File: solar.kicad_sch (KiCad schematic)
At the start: 7 parts

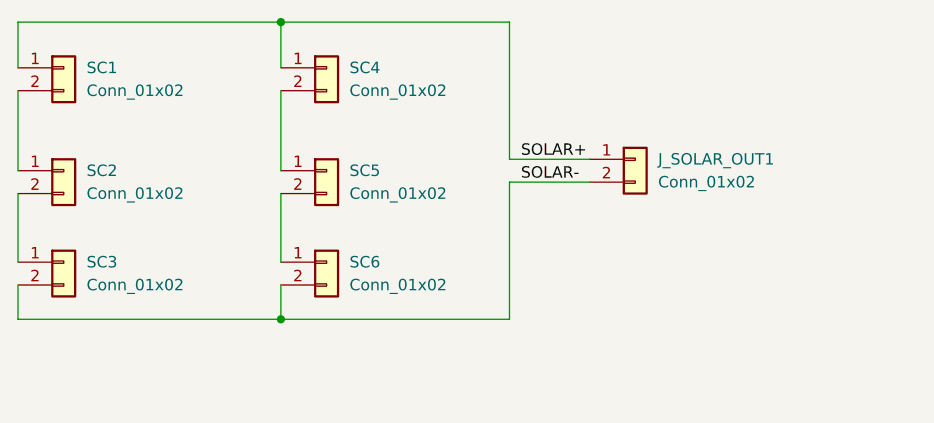
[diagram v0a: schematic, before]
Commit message: add temperature sensor
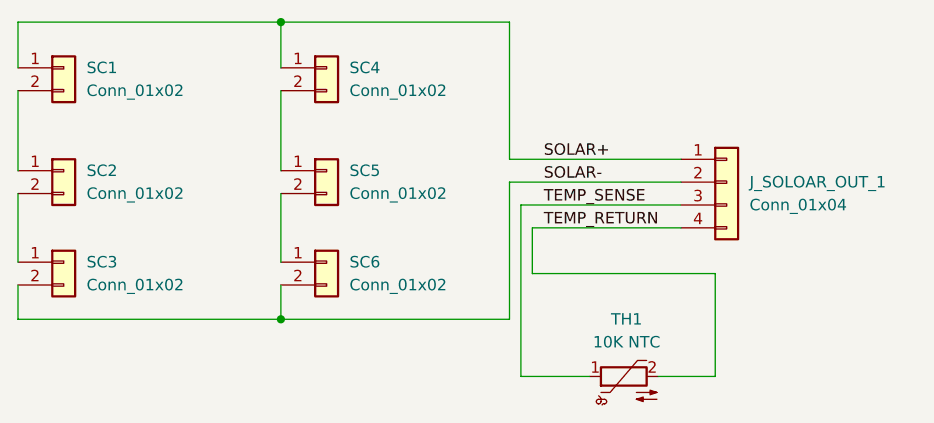
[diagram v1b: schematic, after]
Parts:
- removed J_SOLAR_OUT1: Conn_01x02, Connector_JST:JST_PH_S2B-PH-K_1x02_P2.00mm_Horizontal, symbol Connector_Generic:Conn_01x02
- added J_SOLOAR_OUT_1: Conn_01x04, Connector_JST:JST_PH_S4B-PH-K_1x04_P2.00mm_Horizontal, symbol Connector_Generic:Conn_01x04
- added TH1: 10K NTC, Diode_THT:D_DO-35_SOD27_P7.62mm_Horizontal, symbol Device:Thermistor_NTC
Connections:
- net SOLAR+: now also J_SOLOAR_OUT_1.1 (Pin_1)
- net SOLAR-: now also J_SOLOAR_OUT_1.2 (Pin_2)
- new net TEMP_RETURN: J_SOLOAR_OUT_1.4 (Pin_4), TH1.2
- new net TEMP_SENSE: J_SOLOAR_OUT_1.3 (Pin_3), TH1.1
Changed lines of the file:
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@@
 	(wire
 		(pts
-			(xy 186.69 100.33) (xy 177.8 100.33)
+			(xy 179.07 124.46) (xy 186.69 124.46)
 		)
 		(stroke
@@
 	(wire
 		(pts
+			(xy 200.66 124.46) (xy 200.66 113.03)
+		)
+		(stroke
+			(width 0)
+			(type default)
+		)
+	)
+	(wire
+		(pts
+			(xy 179.07 105.41) (xy 179.07 124.46)
+		)
+		(stroke
+			(width 0)
+			(type default)
+		)
+	)
+	(wire
+		(pts
 			(xy 152.4 114.3) (xy 152.4 118.11)
 		)
@@
 	(wire
 		(pts
+			(xy 180.34 107.95) (xy 196.85 107.95)
+		)
+		(stroke
+			(width 0)
+			(type default)
+		)
+	)
+	(wire
+		(pts
 			(xy 152.4 92.71) (xy 152.4 101.6)
 		)
@@
 	(wire
 		(pts
+			(xy 177.8 102.87) (xy 196.85 102.87)
+		)
+		(stroke
+			(width 0)
+			(type default)
+		)
+	)
+	(wire
+		(pts
+			(xy 194.31 124.46) (xy 200.66 124.46)
+		)
+		(stroke
+			(width 0)
+			(type default)
+		)
+	)
+	(wire
+		(pts
 			(xy 123.19 118.11) (xy 152.4 118.11)
 		)
@@
 	(wire
 		(pts
-			(xy 186.69 102.87) (xy 177.8 102.87)
+			(xy 177.8 100.33) (xy 196.85 100.33)
 		)
 		(stroke
@@
 	(wire
 		(pts
+			(xy 179.07 105.41) (xy 196.85 105.41)
+		)
+		(stroke
+			(width 0)
+			(type default)
+		)
+	)
+	(wire
+		(pts
+			(xy 180.34 113.03) (xy 180.34 107.95)
+		)
+		(stroke
+			(width 0)
+			(type default)
+		)
+	)
+	(wire
+		(pts
+			(xy 200.66 113.03) (xy 180.34 113.03)
+		)
+		(stroke
+			(width 0)
+			(type default)
+		)
+	)
+	(wire
+		(pts
 			(xy 177.8 102.87) (xy 177.8 118.11)
 		)
@@
 		)
 	)
-	(label "SOLAR+"
-		(at 179.07 100.33 0)
+	(label "TEMP_RETURN"
+		(at 181.61 107.95 0)
 		(effects
 			(font
@@
 		)
 	)
+	(label "SOLAR+"
+		(at 181.61 100.33 0)
+		(effects
+			(font
+				(size 1.27 1.27)
+			)
+			(justify left bottom)
+		)
+	)
+	(label "TEMP_SENSE"
+		(at 181.61 105.41 0)
+		(effects
+			(font
+				(size 1.27 1.27)
+			)
+			(justify left bottom)
+		)
+	)
 	(label "SOLAR-"
-		(at 179.07 102.87 0)
+		(at 181.61 102.87 0)
 		(effects
 			(font
@@
 	)
 	(symbol
-		(lib_id "Connector_Generic:Conn_01x02")
-		(at 191.77 100.33 0)
+		(lib_id "Device:Thermistor_NTC")
+		(at 190.5 124.46 90)
 		(unit 1)
 		(body_style 1)
@@
 		(dnp no)
 		(fields_autoplaced yes)
-		(property "Reference" "J_SOLAR_OUT1"
-			(at 194.31 100.3299 0)
-			(show_name no)
-			(do_not_autoplace no)
-			(effects
-				(font
-					(size 1.27 1.27)
-				)
-				(justify left)
-			)
-		)
-		(property "Value" "Conn_01x02"
-			(at 194.31 102.8699 0)
-			(show_name no)
-			(do_not_autoplace no)
-			(effects
-				(font
-					(size 1.27 1.27)
-				)
-				(justify left)
-			)
-		)
-		(property "Footprint" "Connector_JST:JST_PH_S2B-PH-K_1x02_P2.00mm_Horizontal"
-			(at 191.77 100.33 0)
+		(property "Reference" "TH1"
+			(at 190.8175 118.11 90)
+			(show_name no)
+			(do_not_autoplace no)
+			(effects
+				(font
+					(size 1.27 1.27)
+				)
+			)
+		)
+		(property "Value" "10K NTC"
+			(at 190.8175 120.65 90)
+			(show_name no)
+			(do_not_autoplace no)
+			(effects
+				(font
+					(size 1.27 1.27)
+				)
+			)
+		)
+		(property "Footprint" "Diode_THT:D_DO-35_SOD27_P7.62mm_Horizontal"
+			(at 189.23 124.46 0)
 			(hide yes)
 			(show_name no)
@@
 		)
 		(property "Datasheet" ""
-			(at 191.77 100.33 0)
-			(hide yes)
-			(show_name no)
-			(do_not_autoplace no)
-			(effects
-				(font
-					(size 1.27 1.27)
-				)
-			)
-		)
-		(property "Description" "Generic connector, single row, 01x02, script generated (kicad-library-utils/schlib/autogen/connector/)"
-			(at 191.77 100.33 0)
-			(hide yes)
-			(show_name no)
-			(do_not_autoplace no)
-			(effects
-				(font
-					(size 1.27 1.27)
-				)
-			)
+			(at 189.23 124.46 0)
+			(hide yes)
+			(show_name no)
+			(do_not_autoplace no)
+			(effects
+				(font
+					(size 1.27 1.27)
+				)
+			)
+		)
+		(property "Description" "Temperature dependent resistor, negative temperature coefficient"
+			(at 190.5 124.46 0)
+			(hide yes)
+			(show_name no)
+			(do_not_autoplace no)
+			(effects
+				(font
+					(size 1.27 1.27)
+				)
+			)
+		)
+		(pin "1"
 		)
 		(pin "2"
-		)
-		(pin "1"
 		)
 		(instances
 			(project "solar"
 				(path "/1bcf9b9b-31e9-4ffb-9746-b49af780131a"
-					(reference "J_SOLAR_OUT1")
+					(reference "TH1")
 					(unit 1)
 				)
+			)
+		)
+	)
+	(symbol
+		(lib_id "Connector_Generic:Conn_01x04")
+		(at 201.93 102.87 0)
+		(unit 1)
+		(body_style 1)
+		(exclude_from_sim no)
+		(in_bom yes)
+		(on_board yes)
+		(in_pos_files yes)
+		(dnp no)
+		(fields_autoplaced yes)
+		(property "Reference" "J_SOLOAR_OUT_1"
+			(at 204.47 102.8699 0)
+			(show_name no)
+			(do_not_autoplace no)
+			(effects
+				(font
+					(size 1.27 1.27)
+				)
+				(justify left)
+			)
+		)
+		(property "Value" "Conn_01x04"
+			(at 204.47 105.4099 0)
+			(show_name no)
+			(do_not_autoplace no)
+			(effects
+				(font
+					(size 1.27 1.27)
+				)
+				(justify left)
+			)
+		)
+		(property "Footprint" "Connector_JST:JST_PH_S4B-PH-K_1x04_P2.00mm_Horizontal"
+			(at 201.93 102.87 0)
+			(hide yes)
+			(show_name no)
+			(do_not_autoplace no)
+			(effects
+				(font
+					(size 1.27 1.27)
+				)
+			)
+		)
+		(property "Datasheet" ""
+			(at 201.93 102.87 0)
+			(hide yes)
+			(show_name no)
+			(do_not_autoplace no)
+			(effects
+				(font
+					(size 1.27 1.27)
+				)
+			)
+		)
+		(property "Description" "Generic connector, single row, 01x04, script generated (kicad-library-utils/schlib/autogen/connector/)"
+			(at 201.93 102.87 0)
+			(hide yes)
+			(show_name no)
+			(do_not_autoplace no)
+			(effects
+				(font
+					(size 1.27 1.27)
+				)
+			)
+		)
+		(pin "1"
+		)
+		(pin "2"
+		)
+		(pin "3"
+		)
+		(pin "4"
+		)
+		(instances
+			(project "solar"
+				(path "/1bcf9b9b-31e9-4ffb-9746-b49af780131a"
+					(reference "J_SOLOAR_OUT_1")
+					(unit 1)
+				)
